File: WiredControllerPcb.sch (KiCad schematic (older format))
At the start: 28 parts, among them J1 Joystick, J2 Conn_01x06, J3 Conn_01x04, SW1 SW_Push, SW2 SW_Push, SW3 SW_Push, SW4 SW_Push, U1 LP2985-3.3, U2 ATmega328P-MU

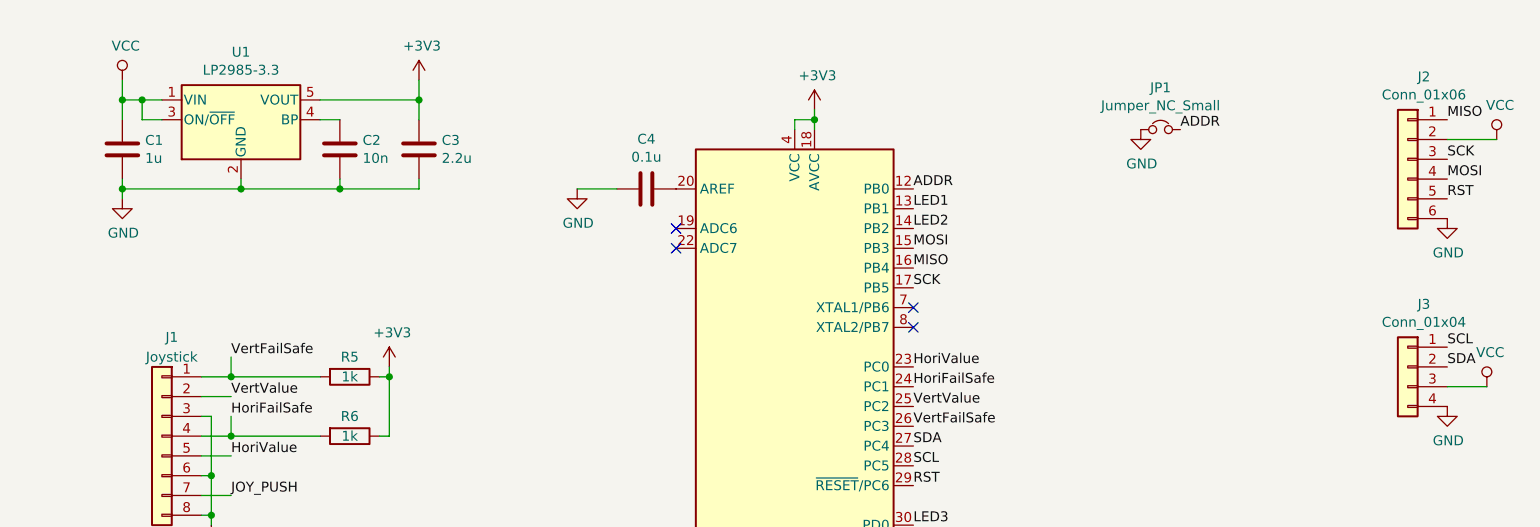
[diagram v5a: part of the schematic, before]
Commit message: Repalce VCC to VCD
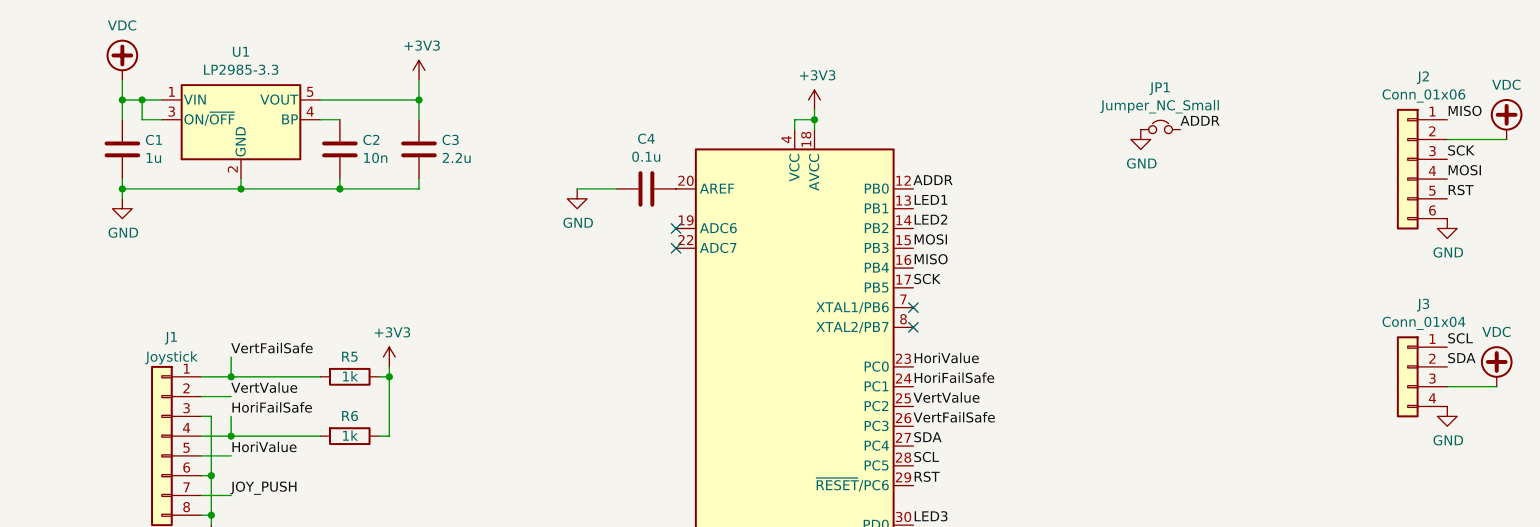
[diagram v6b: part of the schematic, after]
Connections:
- net VCC renamed VDC
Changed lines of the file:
@@
-	1    0    0    -1
-$EndComp
-$Comp
-L power:VCC #PWR0111
-U 1 1 5D2826FD
-P 2450 2050
-F 0 "#PWR0111" H 2450 1900 50  0001 C CNN
-F 1 "VCC" H 2467 2223 50  0000 C CNN
-F 2 "" H 2450 2050 50  0001 C CNN
-F 3 "" H 2450 2050 50  0001 C CNN
-	1    2450 2050
 	1    0    0    -1
 $EndComp
@@
 	1    0    0    -1
 $EndComp
-$Comp
-L power:VCC #PWR0114
-U 1 1 5D2A5908
-P 9400 2350
-F 0 "#PWR0114" H 9400 2200 50  0001 C CNN
-F 1 "VCC" H 9417 2523 50  0000 C CNN
-F 2 "" H 9400 2350 50  0001 C CNN
-F 3 "" H 9400 2350 50  0001 C CNN
-	1    9400 2350
-	1    0    0    -1
-$EndComp
-Wire Wire Line
-	9400 2350 9150 2350
 Text Label 6450 2900 0    50   ~ 0
 MOSI
@@
 $EndComp
 $Comp
-L power:VCC #PWR0115
-U 1 1 5D2AF962
-P 9350 3600
-F 0 "#PWR0115" H 9350 3450 50  0001 C CNN
-F 1 "VCC" H 9367 3773 50  0000 C CNN
-F 2 "" H 9350 3600 50  0001 C CNN
-F 3 "" H 9350 3600 50  0001 C CNN
-	1    9350 3600
-	1    0    0    -1
-$EndComp
-$Comp
 L power:GND #PWR0116
 U 1 1 5D2AFBE1
@@
 	1    0    0    -1
 $EndComp
-Wire Wire Line
-	9350 3600 9150 3600
 Text Label 9150 3500 0    50   ~ 0
 SDA
@@
 NoConn ~ 6450 3200
 NoConn ~ 6450 3300
+$Comp
+L power:VDC #PWR?
+U 1 1 5D7F19B1
+P 2450 2050
+F 0 "#PWR?" H 2450 1950 50  0001 C CNN
+F 1 "VDC" H 2450 2325 50  0000 C CNN
+F 2 "" H 2450 2050 50  0001 C CNN
+F 3 "" H 2450 2050 50  0001 C CNN
+	1    2450 2050
+	1    0    0    -1
+$EndComp
+$Comp
+L power:VDC #PWR?
+U 1 1 5D7F36C1
+P 9450 2350
+F 0 "#PWR?" H 9450 2250 50  0001 C CNN
+F 1 "VDC" H 9450 2625 50  0000 C CNN
+F 2 "" H 9450 2350 50  0001 C CNN
+F 3 "" H 9450 2350 50  0001 C CNN
+	1    9450 2350
+	1    0    0    -1
+$EndComp
+$Comp
+L power:VDC #PWR?
+U 1 1 5D7F3CEB
+P 9400 3600
+F 0 "#PWR?" H 9400 3500 50  0001 C CNN
+F 1 "VDC" H 9400 3875 50  0000 C CNN
+F 2 "" H 9400 3600 50  0001 C CNN
+F 3 "" H 9400 3600 50  0001 C CNN
+	1    9400 3600
+	1    0    0    -1
+$EndComp
+Wire Wire Line
+	9150 3600 9400 3600
+Wire Wire Line
+	9150 2350 9450 2350
 $EndSCHEMATC

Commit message: Add pull up resistors and jumpers for sda and scl
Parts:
- added JP2, JP3: Jumper_NO, Jumper:SolderJumper-2_P1.3mm_Open_RoundedPad1.0x1.5mm, symbol Device:Jumper_NO_Small
- added R7, R8: 1k, Resistor_SMD:R_0603_1608Metric, symbol Device:R
- JP1: value Jumper_NC_Small -> Jumper_NO; symbol Device:Jumper_NC_Small -> Device:Jumper_NO_Small
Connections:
- net +3V3: now also R7.1, R8.1
- net SCL: now also JP3.1
- net SDA: now also JP2.1
- new net: JP2.2, R7.2
- new net: JP3.2, R8.2
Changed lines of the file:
@@
 $EndComp
 $Comp
-L Device:Jumper_NC_Small JP1
+L Device:Jumper_NO_Small JP1
 U 1 1 5D32F173
 P 7700 2300
 F 0 "JP1" H 7700 2512 50  0000 C CNN
-F 1 "Jumper_NC_Small" H 7700 2421 50  0000 C CNN
+F 1 "Jumper_NO" H 7700 2421 50  0000 C CNN
 F 2 "Jumper:SolderJumper-2_P1.3mm_Open_RoundedPad1.0x1.5mm" H 7700 2300 50  0001 C CNN
 F 3 "~" H 7700 2300 50  0001 C CNN
@@
 NoConn ~ 6450 3300
 $Comp
-L power:VDC #PWR?
+L power:VDC #PWR0106
 U 1 1 5D7F19B1
 P 2450 2050
-F 0 "#PWR?" H 2450 1950 50  0001 C CNN
+F 0 "#PWR0106" H 2450 1950 50  0001 C CNN
 F 1 "VDC" H 2450 2325 50  0000 C CNN
 F 2 "" H 2450 2050 50  0001 C CNN
@@
 $EndComp
 $Comp
-L power:VDC #PWR?
+L power:VDC #PWR0111
 U 1 1 5D7F36C1
 P 9450 2350
-F 0 "#PWR?" H 9450 2250 50  0001 C CNN
+F 0 "#PWR0111" H 9450 2250 50  0001 C CNN
 F 1 "VDC" H 9450 2625 50  0000 C CNN
 F 2 "" H 9450 2350 50  0001 C CNN
@@
 $EndComp
 $Comp
-L power:VDC #PWR?
+L power:VDC #PWR0114
 U 1 1 5D7F3CEB
 P 9400 3600
-F 0 "#PWR?" H 9400 3500 50  0001 C CNN
+F 0 "#PWR0114" H 9400 3500 50  0001 C CNN
 F 1 "VDC" H 9400 3875 50  0000 C CNN
 F 2 "" H 9400 3600 50  0001 C CNN
@@
 Wire Wire Line
 	9150 2350 9450 2350
+$Comp
+L power:+3V3 #PWR0115
+U 1 1 5D802349
+P 8050 3300
+F 0 "#PWR0115" H 8050 3150 50  0001 C CNN
+F 1 "+3V3" H 8065 3473 50  0000 C CNN
+F 2 "" H 8050 3300 50  0001 C CNN
+F 3 "" H 8050 3300 50  0001 C CNN
+	1    8050 3300
+	1    0    0    -1
+$EndComp
+$Comp
+L Device:R R7
+U 1 1 5D803072
+P 7850 3400
+F 0 "R7" V 7750 3400 50  0000 C CNN
+F 1 "1k" V 7850 3400 50  0000 C CNN
+F 2 "Resistor_SMD:R_0603_1608Metric" V 7780 3400 50  0001 C CNN
+F 3 "~" H 7850 3400 50  0001 C CNN
+	1    7850 3400
+	0    1    1    0
+$EndComp
+$Comp
+L Device:R R8
+U 1 1 5D806441
+P 7850 3700
+F 0 "R8" V 7750 3700 50  0000 C CNN
+F 1 "1k" V 7850 3700 50  0000 C CNN
+F 2 "Resistor_SMD:R_0603_1608Metric" V 7780 3700 50  0001 C CNN
+F 3 "~" H 7850 3700 50  0001 C CNN
+	1    7850 3700
+	0    1    1    0
+$EndComp
+$Comp
+L Device:Jumper_NO_Small JP2
+U 1 1 5D80699D
+P 7500 3400
+F 0 "JP2" H 7500 3612 50  0000 C CNN
+F 1 "Jumper_NO" H 7500 3521 50  0000 C CNN
+F 2 "Jumper:SolderJumper-2_P1.3mm_Open_RoundedPad1.0x1.5mm" H 7500 3400 50  0001 C CNN
+F 3 "~" H 7500 3400 50  0001 C CNN
+	1    7500 3400
+	1    0    0    -1
+$EndComp
+$Comp
+L Device:Jumper_NO_Small JP3
+U 1 1 5D808A21
+P 7500 3700
+F 0 "JP3" H 7500 3912 50  0000 C CNN
+F 1 "Jumper_NO" H 7500 3821 50  0000 C CNN
+F 2 "Jumper:SolderJumper-2_P1.3mm_Open_RoundedPad1.0x1.5mm" H 7500 3700 50  0001 C CNN
+F 3 "~" H 7500 3700 50  0001 C CNN
+	1    7500 3700
+	1    0    0    -1
+$EndComp
+Text Label 7400 3400 2    50   ~ 0
+SDA
+Text Label 7400 3700 2    50   ~ 0
+SCL
+Wire Wire Line
+	7600 3700 7700 3700
+Wire Wire Line
+	7700 3400 7600 3400
+Wire Wire Line
+	8000 3400 8050 3400
+Wire Wire Line
+	8050 3400 8050 3300
+Wire Wire Line
+	8050 3400 8050 3700
+Wire Wire Line
+	8050 3700 8000 3700
+Connection ~ 8050 3400
 $EndSCHEMATC

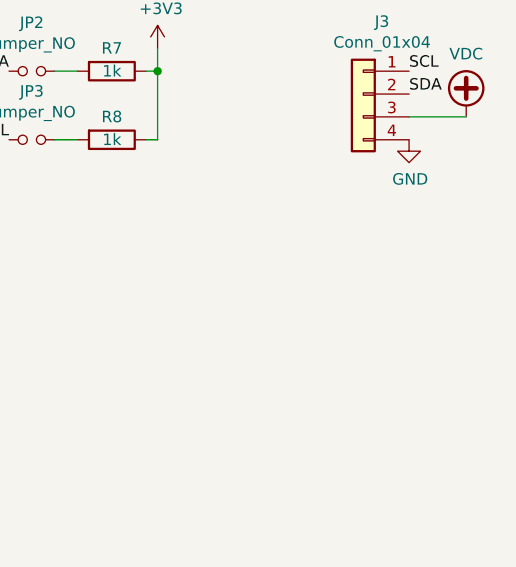
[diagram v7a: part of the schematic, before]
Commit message: Add terminal block
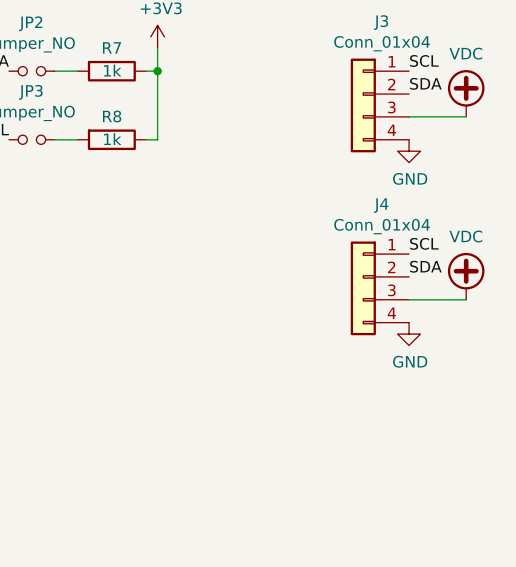
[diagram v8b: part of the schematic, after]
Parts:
- added J4: Conn_01x04, TerminalBlock:TerminalBlock_bornier-4_P5.08mm, symbol Connector_Generic:Conn_01x04
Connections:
- net GND: now also J4.4 (Pin_4)
- net SCL: now also J4.1 (Pin_1)
- net SDA: now also J4.2 (Pin_2)
- net VDC: now also J4.3 (Pin_3)
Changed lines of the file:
@@
 	8050 3700 8000 3700
 Connection ~ 8050 3400
+$Comp
+L Connector_Generic:Conn_01x04 J4
+U 1 1 5D81B9BA
+P 8950 4300
+F 0 "J4" H 8868 4617 50  0000 C CNN
+F 1 "Conn_01x04" H 8868 4526 50  0000 C CNN
+F 2 "TerminalBlock:TerminalBlock_bornier-4_P5.08mm" H 8950 4300 50  0001 C CNN
+F 3 "~" H 8950 4300 50  0001 C CNN
+	1    8950 4300
+	-1   0    0    -1
+$EndComp
+$Comp
+L power:GND #PWR0121
+U 1 1 5D81B9C0
+P 9150 4500
+F 0 "#PWR0121" H 9150 4250 50  0001 C CNN
+F 1 "GND" H 9155 4327 50  0000 C CNN
+F 2 "" H 9150 4500 50  0001 C CNN
+F 3 "" H 9150 4500 50  0001 C CNN
+	1    9150 4500
+	1    0    0    -1
+$EndComp
+Text Label 9150 4300 0    50   ~ 0
+SDA
+Text Label 9150 4200 0    50   ~ 0
+SCL
+$Comp
+L power:VDC #PWR0122
+U 1 1 5D81B9C8
+P 9400 4400
+F 0 "#PWR0122" H 9400 4300 50  0001 C CNN
+F 1 "VDC" H 9400 4675 50  0000 C CNN
+F 2 "" H 9400 4400 50  0001 C CNN
+F 3 "" H 9400 4400 50  0001 C CNN
+	1    9400 4400
+	1    0    0    -1
+$EndComp
+Wire Wire Line
+	9150 4400 9400 4400
 $EndSCHEMATC
